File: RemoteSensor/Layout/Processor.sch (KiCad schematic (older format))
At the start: 21 parts, among them J3 LCD_HEADER, Q3 2N7002, SW2 SW_Push, U7 ESP-12F, U8 LM50CIM3, U9 MCP23008-E_P

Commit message: Update outputs
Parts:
- SW2: value SW_Push -> FLASH
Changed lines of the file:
@@
 P 2100 1300
 F 0 "SW2" H 2100 1585 50  0000 C CNN
-F 1 "SW_Push" H 2100 1494 50  0000 C CNN
+F 1 "FLASH" H 2100 1494 50  0000 C CNN
 F 2 "Button_Switch_SMD:SW_SPST_TL3342" H 2100 1500 50  0001 C CNN
 F 3 "~" H 2100 1500 50  0001 C CNN

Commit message: Change what pins are used for i2c
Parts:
- D1, D2: symbol Device:LED -> RemoteSensor-rescue:LED-Device
- J3: symbol Connector_Generic:Conn_01x04 -> RemoteSensor-rescue:Conn_01x04-Connector_Generic
- R11, R12, R13, R14, R15, R16, R17, R18, R19, R20, R21, R22: symbol Device:R_US -> RemoteSensor-rescue:R_US-Device
- SW2: symbol Switch:SW_Push -> RemoteSensor-rescue:SW_Push-Switch
- U7: symbol RF_Module:ESP-12F -> RemoteSensor-rescue:ESP-12F-RF_Module
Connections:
- net labels removed: SLEEP_STS
- wire segments 83 -> 81
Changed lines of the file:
@@
 Comment4 ""
 $EndDescr
-Text Label 4250 2850 0    50   ~ 0
-SDA
-Text Label 4250 2750 0    50   ~ 0
-SCL
-Wire Wire Line
-	5000 2850 4250 2850
-Wire Wire Line
-	5000 2750 4250 2750
 Text Label 4450 2350 0    50   ~ 0
 TEMP_PIN
@@
 	4650 1800 4650 1950
 $Comp
-L Device:R_US R?
+L RemoteSensor-rescue:R_US-Device R?
 U 1 1 5EF69133
 P 4150 1650
@@
 $EndComp
 $Comp
-L RF_Module:ESP-12F U?
+L RemoteSensor-rescue:ESP-12F-RF_Module U?
 U 1 1 5EF6913A
 P 5600 2550
@@
 Connection ~ 4650 1500
 $Comp
-L Device:R_US R?
+L RemoteSensor-rescue:R_US-Device R?
 U 1 1 5EF69149
 P 4650 1650
@@
 	8750 2750 8750 3150
 $Comp
-L Device:R_US R?
+L RemoteSensor-rescue:R_US-Device R?
 U 1 1 5EF7CD26
 P 9450 3900
@@
 $EndComp
 $Comp
-L Device:R_US R?
+L RemoteSensor-rescue:R_US-Device R?
 U 1 1 5EF7CD2C
 P 9450 4250
@@
 Wire Wire Line
 	6200 2250 6550 2250
-Wire Wire Line
-	6200 2350 6550 2350
-Wire Wire Line
-	6200 2450 6550 2450
 Wire Wire Line
 	6200 2550 6550 2550
@@
 	5400 5050 5800 5050
 $Comp
-L Device:R_US R19
+L RemoteSensor-rescue:R_US-Device R19
 U 1 1 5EF1D3A2
 P 5000 5400
@@
 $EndComp
 $Comp
-L Device:R_US R20
+L RemoteSensor-rescue:R_US-Device R20
 U 1 1 5EF20C41
 P 7000 1650
@@
 	6200 2150 7000 2150
 $Comp
-L Device:R_US R21
+L RemoteSensor-rescue:R_US-Device R21
 U 1 1 5EF266EA
 P 7000 3000
@@
 Wire Wire Line
 	5300 4750 5800 4750
-Text GLabel 6550 2350 2    50   Input ~ 0
-HB_PIN
-Text GLabel 6550 2450 2    50   Input ~ 0
-BATT_PIN
 Text GLabel 6550 2550 2    50   Input ~ 0
 SLEEP_PIN
 Text GLabel 5300 4850 0    50   Input ~ 0
-SLEEP_STS
+HB_PIN
 Text GLabel 5300 4950 0    50   Input ~ 0
-WAKE_STS
+BATT_PIN
 Wire Wire Line
 	5300 4850 5800 4850
@@
 	5600 1500 6450 1500
 $Comp
-L Device:R_US R22
+L RemoteSensor-rescue:R_US-Device R22
 U 1 1 5EF17614
 P 6450 1650
@@
 DOWN_BTN
 $Comp
-L Switch:SW_Push SW2
+L RemoteSensor-rescue:SW_Push-Switch SW2
 U 1 1 5EF8556A
 P 2100 1300
+AR Path="/5EF8556A" Ref="SW2"  Part="1"
+AR Path="/5EF5F91F/5EF8556A" Ref="SW2"  Part="1"
 F 0 "SW2" H 2100 1585 50  0000 C CNN
 F 1 "FLASH" H 2100 1494 50  0000 C CNN
@@
 	2500 6350 2650 6350
 $Comp
-L Device:R_US R?
+L RemoteSensor-rescue:R_US-Device R?
 U 1 1 5EF7FA3A
 P 2350 6350
@@
 $EndComp
 $Comp
-L Device:R_US R?
+L RemoteSensor-rescue:R_US-Device R?
 U 1 1 5EF7FA34
 P 2350 5950
@@
 	2950 5950 3150 5950
 $Comp
-L Device:LED D?
+L RemoteSensor-rescue:LED-Device D?
 U 1 1 5EF7FA23
 P 2800 6350
@@
 $EndComp
 $Comp
-L Device:LED D?
+L RemoteSensor-rescue:LED-Device D?
 U 1 1 5EF7FA1D
 P 2800 5950
@@
 $EndComp
 $Comp
-L Connector_Generic:Conn_01x04 J?
+L RemoteSensor-rescue:Conn_01x04-Connector_Generic J?
 U 1 1 5EF6FC1C
 P 2750 4000
@@
 $EndComp
 $Comp
-L Device:R_US R?
+L RemoteSensor-rescue:R_US-Device R?
 U 1 1 5EF6D21F
 P 2800 2650
@@
 $EndComp
 $Comp
-L Device:R_US R?
+L RemoteSensor-rescue:R_US-Device R?
 U 1 1 5EF6D219
 P 2200 2650
@@
 $EndComp
 $Comp
-L SparkFun-PowerSymbols:GND #GND0123
+L RemoteSensor-rescue:GND-SparkFun-PowerSymbols #GND0123
 U 1 1 5EF95E82
 P 2550 1300
+AR Path="/5EF95E82" Ref="#GND0123"  Part="1"
+AR Path="/5EF5F91F/5EF95E82" Ref="#GND0123"  Part="1"
 F 0 "#GND0123" H 2600 1250 45  0001 L BNN
 F 1 "GND" H 2550 1130 45  0000 C CNN
@@
 Wire Wire Line
 	1650 1300 1900 1300
+Wire Wire Line
+	6200 2350 6500 2350
+Wire Wire Line
+	6200 2450 6500 2450
+Text Label 6500 2350 2    50   ~ 0
+SCL
+Text Label 6500 2450 2    50   ~ 0
+SDA
 $EndSCHEMATC

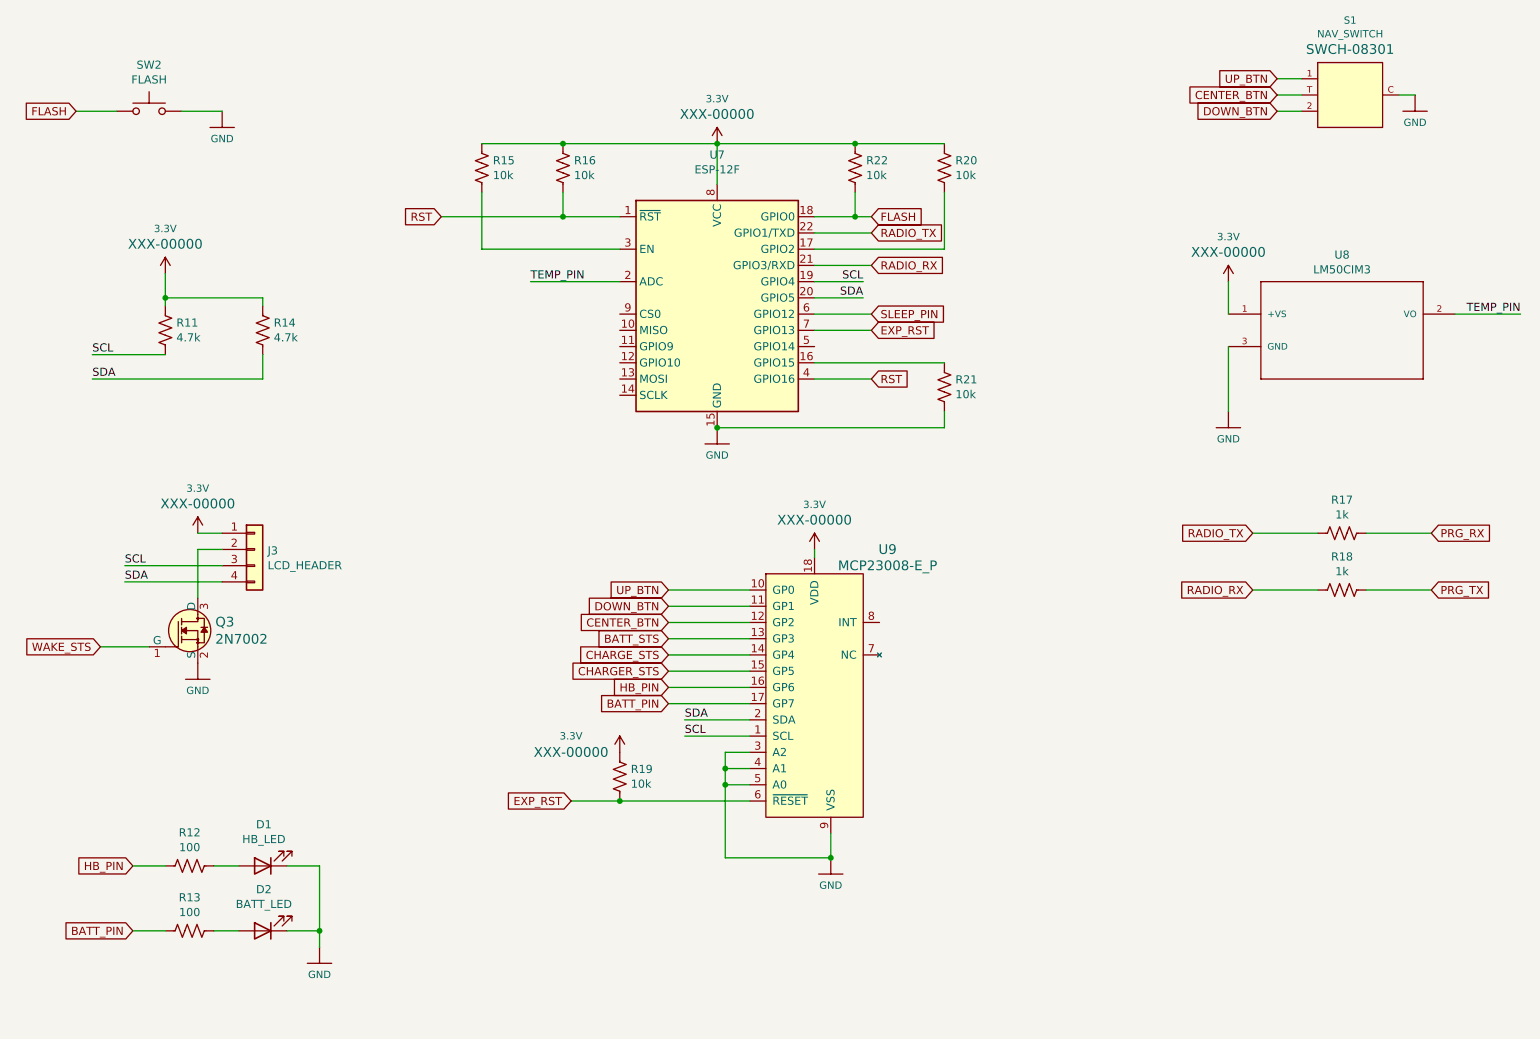
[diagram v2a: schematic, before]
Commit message: Change how power is switched between battery and USB
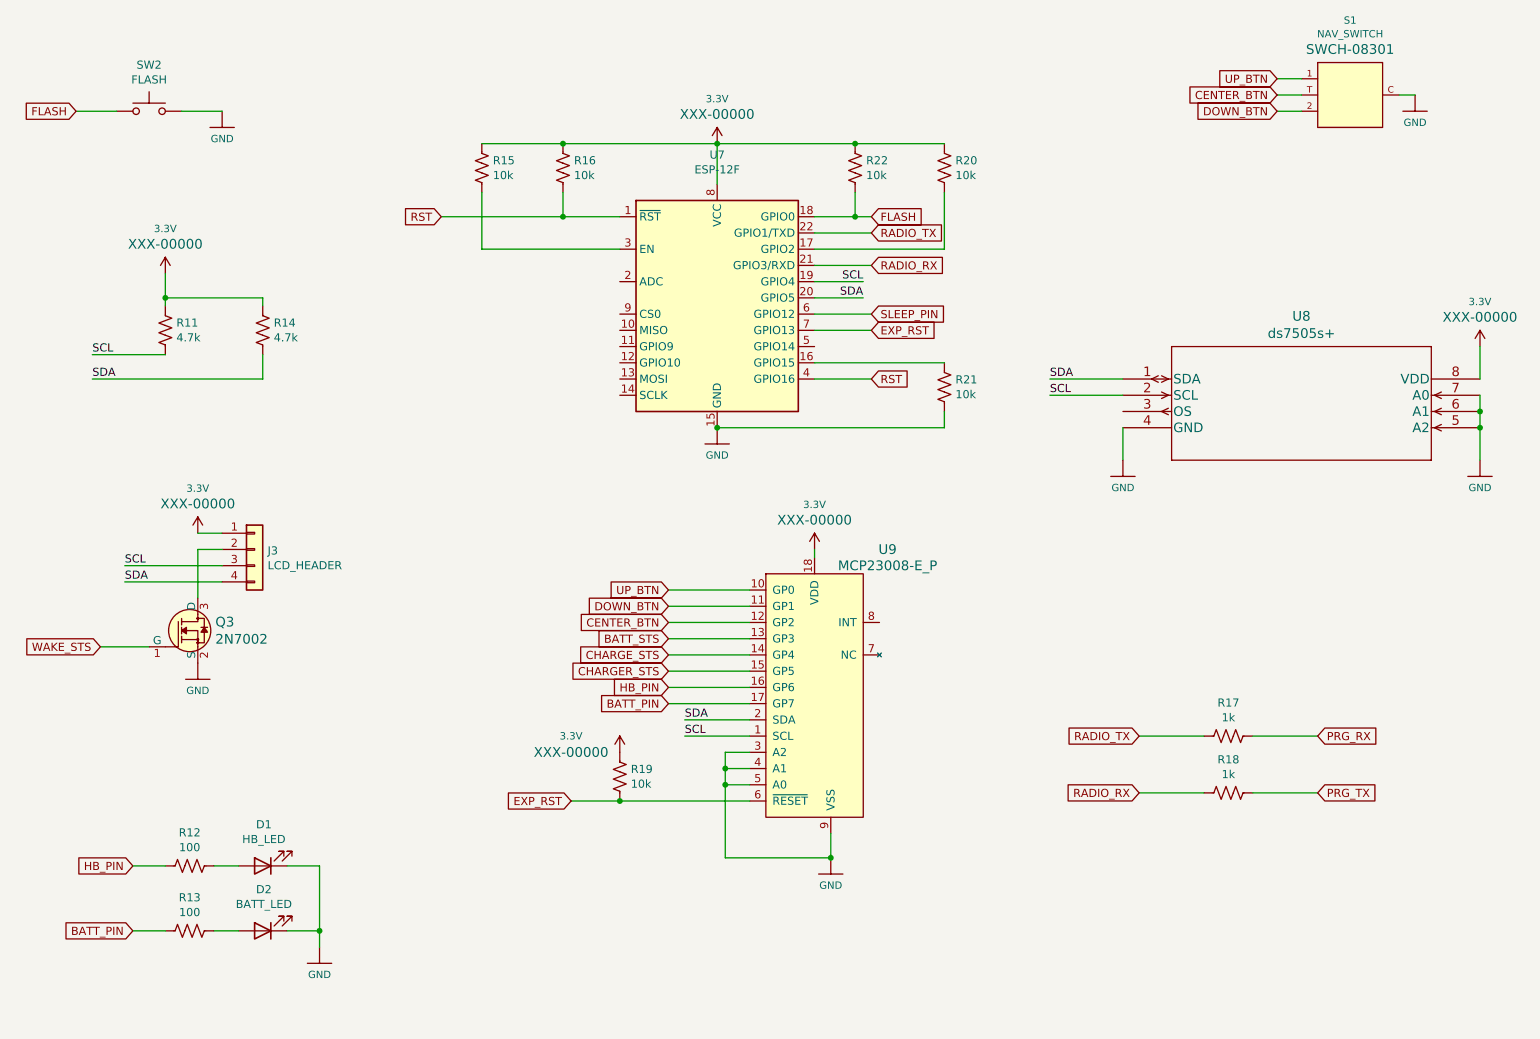
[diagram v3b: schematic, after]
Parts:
- removed U8: LM50CIM3, SOT95P260X110-3N, symbol RemoteSensor-rescue:LM50CIM3-LM50CIM3
- added U8: ds7505s+, Package_SO:SOIC-8_3.9x4.9mm_P1.27mm, symbol ds7505s:ds7505s+
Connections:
- net 3.3V: now also U8.8 (VDD)
- net GND: now also U8.4 (GND), U8.5 (A2), U8.6 (A1), U8.7 (A0)
- net SCL: now also U8.2 (SCL)
- net SDA: now also U8.1 (SDA)
- net TEMP_PIN: no longer names the net of U7.2 (ADC)
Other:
- moved on the sheet: R17, R18
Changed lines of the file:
@@
 Comment4 ""
 $EndDescr
-Text Label 4450 2350 0    50   ~ 0
-TEMP_PIN
-Wire Wire Line
-	5000 2350 4450 2350
 $Comp
 L RemoteSensor-rescue:3.3V-SparkFun-PowerSymbols #SUPPLY?
@@
 	9800 1200 9900 1200
 $Comp
-L RemoteSensor-rescue:LM50CIM3-LM50CIM3 U?
-U 1 1 5EF73CDC
-P 9450 2550
-AR Path="/5EF73CDC" Ref="U?"  Part="1"
-AR Path="/5EF5F91F/5EF73CDC" Ref="U8"  Part="1"
-F 0 "U8" H 9450 2915 50  0000 C CNN
-F 1 "LM50CIM3" H 9450 2824 50  0000 C CNN
-F 2 "SOT95P260X110-3N" H 9450 2550 50  0001 L BNN
-F 3 "" H 9450 2550 50  0001 L BNN
-F 4 "LM50CIM3/NOPBCT-ND" H 9450 2550 50  0001 L BNN "Field4"
-F 5 "Texas Instruments" H 9450 2550 50  0001 L BNN "Field5"
-F 6 "https://www.digikey.com/product-detail/en/texas-instruments/LM50CIM3-NOPB/LM50CIM3-NOPBCT-ND/120169?utm_source=snapeda&utm_medium=aggregator&utm_campaign=symbol" H 9450 2550 50  0001 L BNN "Field6"
-F 7 "LM50CIM3/NOPB" H 9450 2550 50  0001 L BNN "Field7"
-F 8 "SOT-23 Texas Instruments" H 9450 2550 50  0001 L BNN "Field8"
-	1    9450 2550
-	1    0    0    -1
-$EndComp
-$Comp
-L RemoteSensor-rescue:3.3V-SparkFun-PowerSymbols #SUPPLY?
-U 1 1 5EF73CE2
-P 8750 2350
-AR Path="/5EF73CE2" Ref="#SUPPLY?"  Part="1"
-AR Path="/5EF5F91F/5EF73CE2" Ref="#SUPPLY0119"  Part="1"
-F 0 "#SUPPLY0119" H 8800 2350 45  0001 L BNN
-F 1 "3.3V" H 8750 2626 45  0000 C CNN
-F 2 "XXX-00000" H 8750 2531 60  0000 C CNN
-F 3 "" H 8750 2350 60  0001 C CNN
-	1    8750 2350
-	1    0    0    -1
-$EndComp
-Wire Wire Line
-	8750 2550 8750 2350
-$Comp
-L RemoteSensor-rescue:GND-SparkFun-PowerSymbols #GND?
-U 1 1 5EF73CE9
-P 8750 3150
-AR Path="/5EF73CE9" Ref="#GND?"  Part="1"
-AR Path="/5EF5F91F/5EF73CE9" Ref="#GND0117"  Part="1"
-F 0 "#GND0117" H 8800 3100 45  0001 L BNN
-F 1 "GND" H 8750 2980 45  0000 C CNN
-F 2 "" H 8750 3050 60  0001 C CNN
-F 3 "" H 8750 3050 60  0001 C CNN
-	1    8750 3150
-	1    0    0    -1
-$EndComp
-Text Label 10550 2550 2    50   ~ 0
-TEMP_PIN
-Wire Wire Line
-	10150 2550 10550 2550
-Wire Wire Line
-	8750 2750 8750 3150
-$Comp
 L RemoteSensor-rescue:R_US-Device R?
 U 1 1 5EF7CD26
-P 9450 3900
+P 8750 5150
 AR Path="/5EF7CD26" Ref="R?"  Part="1"
 AR Path="/5EF5F91F/5EF7CD26" Ref="R17"  Part="1"
-F 0 "R17" V 9245 3900 50  0000 C CNN
-F 1 "1k" V 9336 3900 50  0000 C CNN
-F 2 "Resistor_SMD:R_0603_1608Metric_Pad1.05x0.95mm_HandSolder" V 9490 3890 50  0001 C CNN
-F 3 "~" H 9450 3900 50  0001 C CNN
-	1    9450 3900
+F 0 "R17" V 8545 5150 50  0000 C CNN
+F 1 "1k" V 8636 5150 50  0000 C CNN
+F 2 "Resistor_SMD:R_0603_1608Metric_Pad1.05x0.95mm_HandSolder" V 8790 5140 50  0001 C CNN
+F 3 "~" H 8750 5150 50  0001 C CNN
+	1    8750 5150
 	0    1    1    0
 $EndComp
@@
 L RemoteSensor-rescue:R_US-Device R?
 U 1 1 5EF7CD2C
-P 9450 4250
+P 8750 5500
 AR Path="/5EF7CD2C" Ref="R?"  Part="1"
 AR Path="/5EF5F91F/5EF7CD2C" Ref="R18"  Part="1"
-F 0 "R18" V 9245 4250 50  0000 C CNN
-F 1 "1k" V 9336 4250 50  0000 C CNN
-F 2 "Resistor_SMD:R_0603_1608Metric_Pad1.05x0.95mm_HandSolder" V 9490 4240 50  0001 C CNN
-F 3 "~" H 9450 4250 50  0001 C CNN
-	1    9450 4250
+F 0 "R18" V 8545 5500 50  0000 C CNN
+F 1 "1k" V 8636 5500 50  0000 C CNN
+F 2 "Resistor_SMD:R_0603_1608Metric_Pad1.05x0.95mm_HandSolder" V 8790 5490 50  0001 C CNN
+F 3 "~" H 8750 5500 50  0001 C CNN
+	1    8750 5500
 	0    1    1    0
 $EndComp
@@
 Wire Wire Line
 	9050 1300 9200 1300
-Text GLabel 8900 3900 0    50   Input ~ 0
+Text GLabel 8200 5150 0    50   Input ~ 0
 RADIO_TX
-Text GLabel 8900 4250 0    50   Input ~ 0
+Text GLabel 8200 5500 0    50   Input ~ 0
 RADIO_RX
 Wire Wire Line
-	8900 4250 9300 4250
-Wire Wire Line
-	8900 3900 9300 3900
+	8200 5500 8600 5500
+Wire Wire Line
+	8200 5150 8600 5150
 Wire Wire Line
 	6200 2050 6550 2050
@@
 Text GLabel 6550 1950 2    50   Input ~ 0
 FLASH
-Text GLabel 10000 3900 2    50   Input ~ 0
+Text GLabel 9300 5150 2    50   Input ~ 0
 PRG_RX
-Text GLabel 10000 4250 2    50   Input ~ 0
+Text GLabel 9300 5500 2    50   Input ~ 0
 PRG_TX
 Wire Wire Line
-	9600 3900 10000 3900
-Wire Wire Line
-	9600 4250 10000 4250
+	8900 5150 9300 5150
+Wire Wire Line
+	8900 5500 9300 5500
 Text GLabel 5300 4350 0    50   Input ~ 0
 DOWN_BTN
@@
 Text Label 6500 2450 2    50   ~ 0
 SDA
+$Comp
+L ds7505s:ds7505s+ U8
+U 1 1 5F5D9C9D
+P 8100 2950
+F 0 "U8" H 9200 3337 60  0000 C CNN
+F 1 "ds7505s+" H 9200 3231 60  0000 C CNN
+F 2 "Package_SO:SOIC-8_3.9x4.9mm_P1.27mm" H 9200 3190 60  0001 C CNN
+F 3 "" H 8100 2950 60  0000 C CNN
+	1    8100 2950
+	1    0    0    -1
+$EndComp
+$Comp
+L SparkFun-PowerSymbols:3.3V #SUPPLY0119
+U 1 1 5F5DA98D
+P 10300 2750
+F 0 "#SUPPLY0119" H 10350 2750 45  0001 L BNN
+F 1 "3.3V" H 10300 3026 45  0000 C CNN
+F 2 "XXX-00000" H 10300 2931 60  0000 C CNN
+F 3 "" H 10300 2750 60  0001 C CNN
+	1    10300 2750
+	1    0    0    -1
+$EndComp
+$Comp
+L SparkFun-PowerSymbols:GND #GND0117
+U 1 1 5F5DB10E
+P 8100 3450
+F 0 "#GND0117" H 8150 3400 45  0001 L BNN
+F 1 "GND" H 8100 3280 45  0000 C CNN
+F 2 "" H 8100 3350 60  0001 C CNN
+F 3 "" H 8100 3350 60  0001 C CNN
+	1    8100 3450
+	1    0    0    -1
+$EndComp
+Wire Wire Line
+	8100 3450 8100 3250
+Wire Wire Line
+	10300 2750 10300 2950
+Wire Wire Line
+	10300 3050 10300 3150
+Wire Wire Line
+	10300 3150 10300 3250
+Connection ~ 10300 3150
+$Comp
+L SparkFun-PowerSymbols:GND #GND0120
+U 1 1 5F5E5DFF
+P 10300 3450
+F 0 "#GND0120" H 10350 3400 45  0001 L BNN
+F 1 "GND" H 10300 3280 45  0000 C CNN
+F 2 "" H 10300 3350 60  0001 C CNN
+F 3 "" H 10300 3350 60  0001 C CNN
+	1    10300 3450
+	1    0    0    -1
+$EndComp
+Wire Wire Line
+	10300 3450 10300 3250
+Connection ~ 10300 3250
+Wire Wire Line
+	8100 2950 7650 2950
+Wire Wire Line
+	8100 3050 7650 3050
+Text Label 7650 2950 0    50   ~ 0
+SDA
+Text Label 7650 3050 0    50   ~ 0
+SCL
 $EndSCHEMATC
